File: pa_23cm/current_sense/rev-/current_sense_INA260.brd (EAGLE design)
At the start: 69.8 x 69.8 mm, 34 parts, among them IC1 INA260, IC2 MCP9700

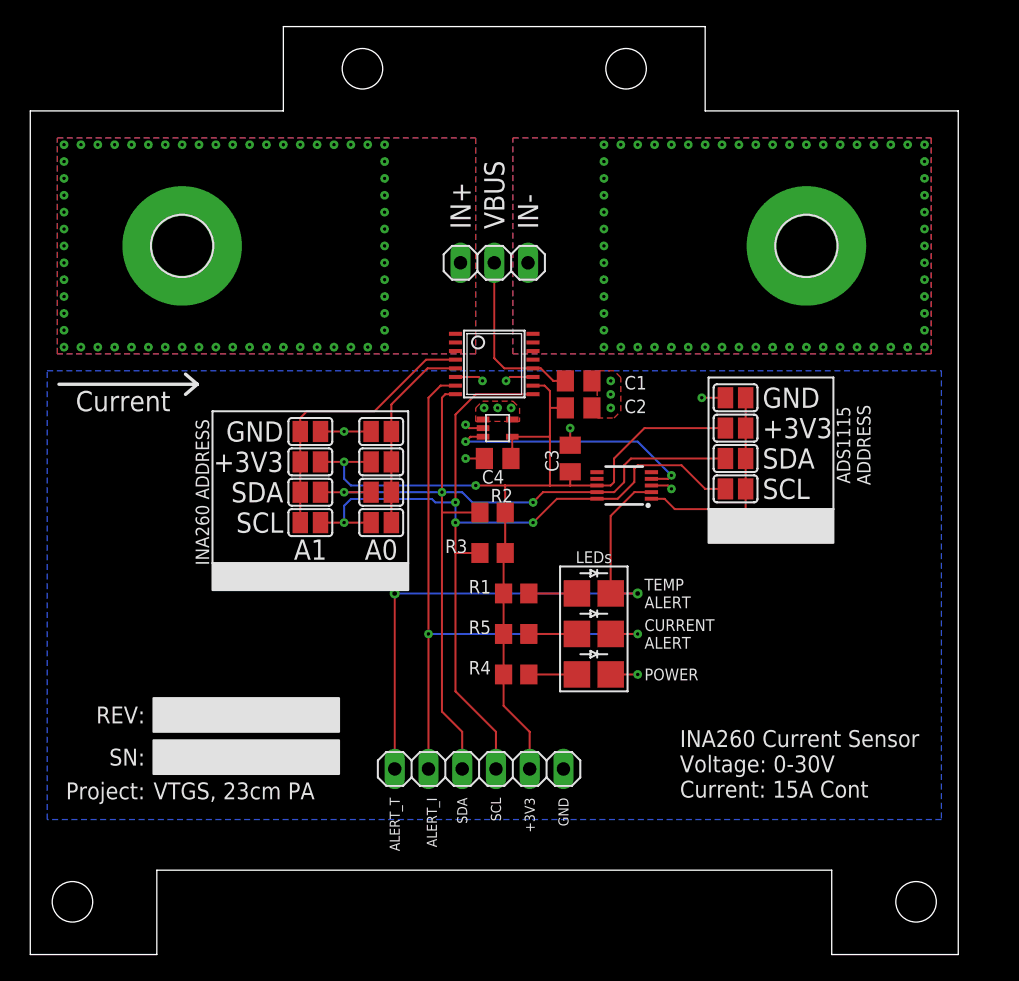
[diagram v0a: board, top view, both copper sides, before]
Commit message: added Analog Input breakout for ADS1115 ADC.
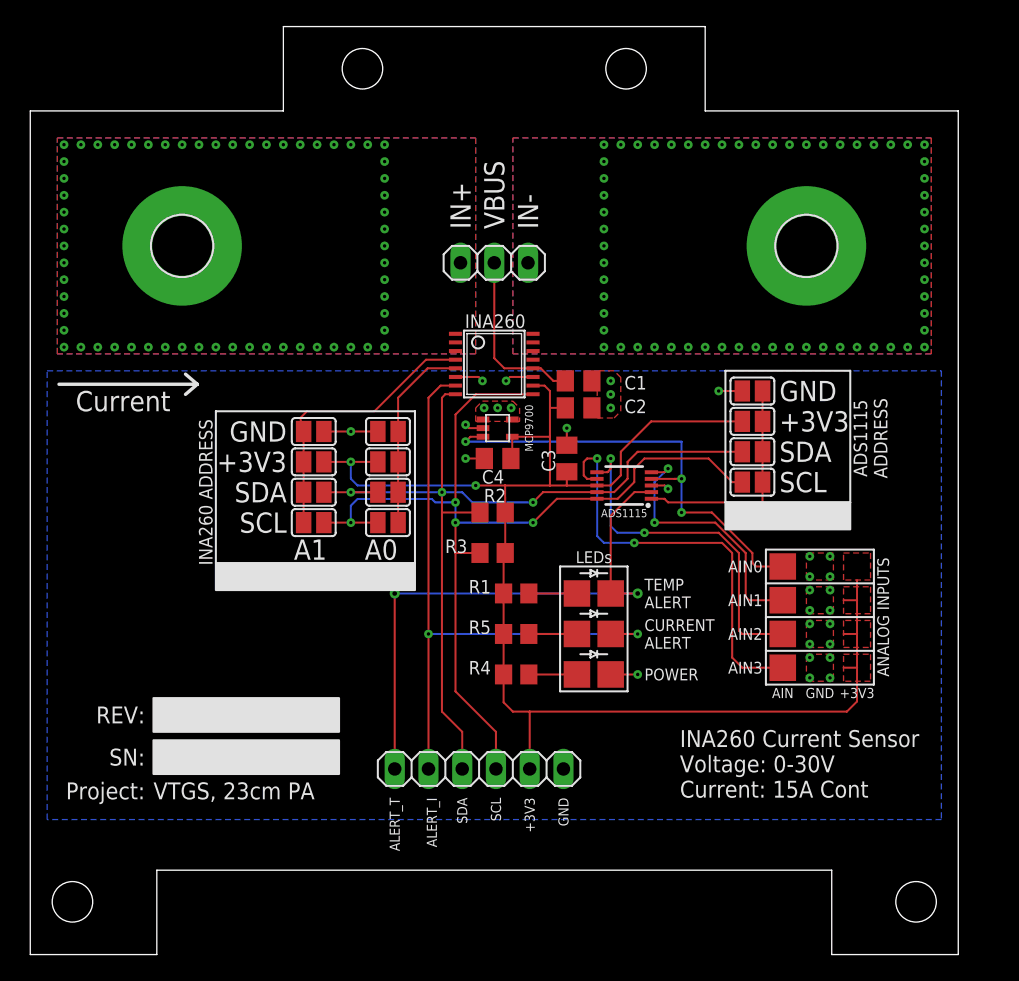
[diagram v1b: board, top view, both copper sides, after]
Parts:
- added AIN0, AIN1, AIN2, AIN3: TPSQTP20SQ, testpad:TP20SQ
- moved SJ12 1.37 mm to (54.4, 35.6)
- moved SJ9 1.37 mm to (54.4, 42.4)
- moved SJ10 1.37 mm to (54.4, 40.1)
- moved SJ11 1.37 mm to (54.4, 37.8)
- moved SJ5 0.51 mm to (26.9, 39.4)
- moved SJ6 0.51 mm to (26.9, 37.1)
- moved SJ7 0.51 mm to (26.9, 34.8)
- moved SJ8 0.51 mm to (26.9, 32.5)
- moved C3 0.25 mm to (40.4, 37.3)
- moved SJ1 0.25 mm to (21.3, 39.4)
- moved SJ2 0.25 mm to (21.3, 37.1)
- moved SJ3 0.25 mm to (21.3, 34.8)
- moved SJ4 0.25 mm to (21.3, 32.5)
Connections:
- new net AIN1: ADC1.5, AIN1.TP
- new net AIN2: ADC1.6, AIN2.TP
- new net AIN3: ADC1.7, AIN3.TP
- net V_TEMP: now also AIN0.TP
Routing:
- net +3V3: track 74.3 -> 113.4 mm
- net AIN3: track 0.00 -> 31.8 mm, vias 0 -> 2
- net AIN2: track 0.00 -> 26.7 mm, vias 0 -> 2
- net AIN1: track 0.00 -> 19.9 mm, vias 0 -> 2
- net V_TEMP: track 19.6 -> 35.1 mm, vias 2 -> 3
- net SDA: track 67.5 -> 68.7 mm
- net SCL: track 73.5 -> 74.7 mm
- net ADDR: track 15.8 -> 16.9 mm
- net GND: vias 15 -> 31
- added copper zone on layer 1, net +3V3
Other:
- board text added: "AIN"
- board text added: "ANALOG INPUTS"
